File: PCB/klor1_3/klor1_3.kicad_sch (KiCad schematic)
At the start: 85 parts, among them J1 MJ-4PP-9, J2 Haptic Buzz, SW1 SW_PUSH-MX_W_LED, SW10 SW_PUSH-MX_W_LED, SW11 SW_PUSH-MX_W_LED, SW12 SW_PUSH-MX_W_LED, SW13 SW_PUSH-MX_W_LED, SW14 SW_PUSH-MX_W_LED, SW15 SW_PUSH-MX_W_LED, SW16 SW_PUSH-MX_W_LED, SW17 SW_PUSH-MX_W_LED, SW18 RotaryEncoder_Switch, SW19 SW_PUSH-MX_W_LED, SW2 SW_PUSH-MX_W_LED, SW20 SW_PUSH-MX_W_LED, SW21 SW_PUSH-MX_W_LED, SW23 5Way-Tactile_K1-1506DN-01, SW3 SW_PUSH-MX_W_LED, SW4 SW_PUSH-MX_W_LED, SW5 SW_PUSH-MX_W_LED, SW6 SW_PUSH-MX_W_LED, SW7 SW_PUSH-MX_W_LED, SW8 SW_PUSH-MX_W_LED, SW9 SW_PUSH-MX_W_LED, U1 ProMicro

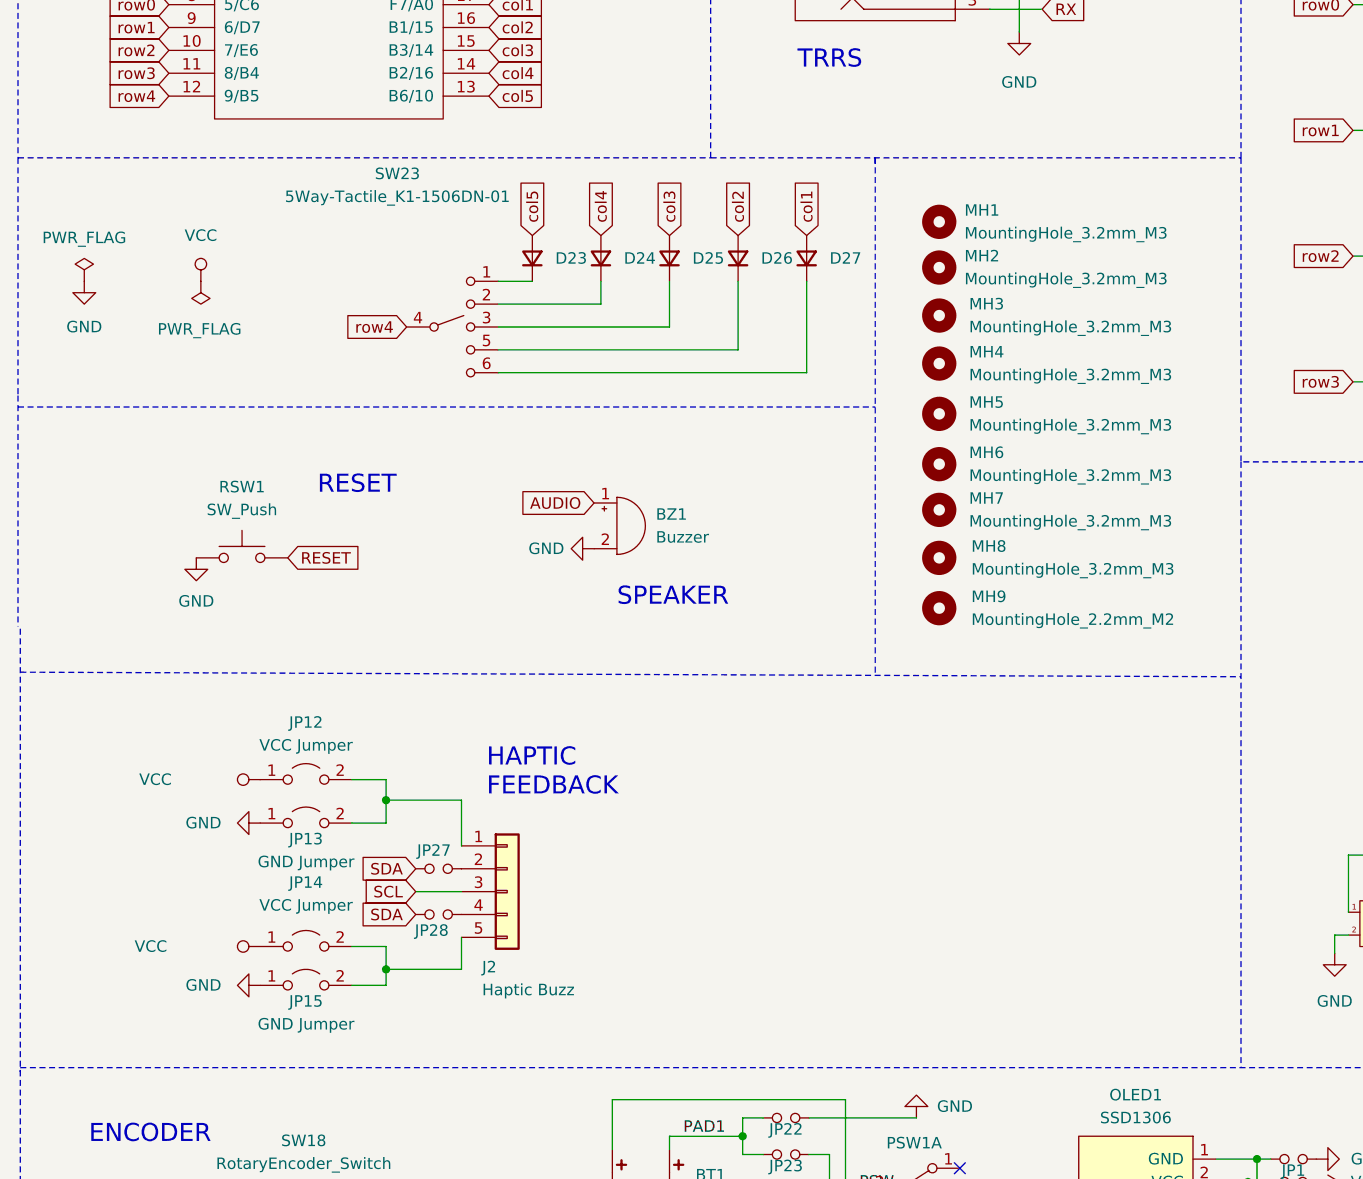
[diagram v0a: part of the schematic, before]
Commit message: move and add label for 5way switch in schematic
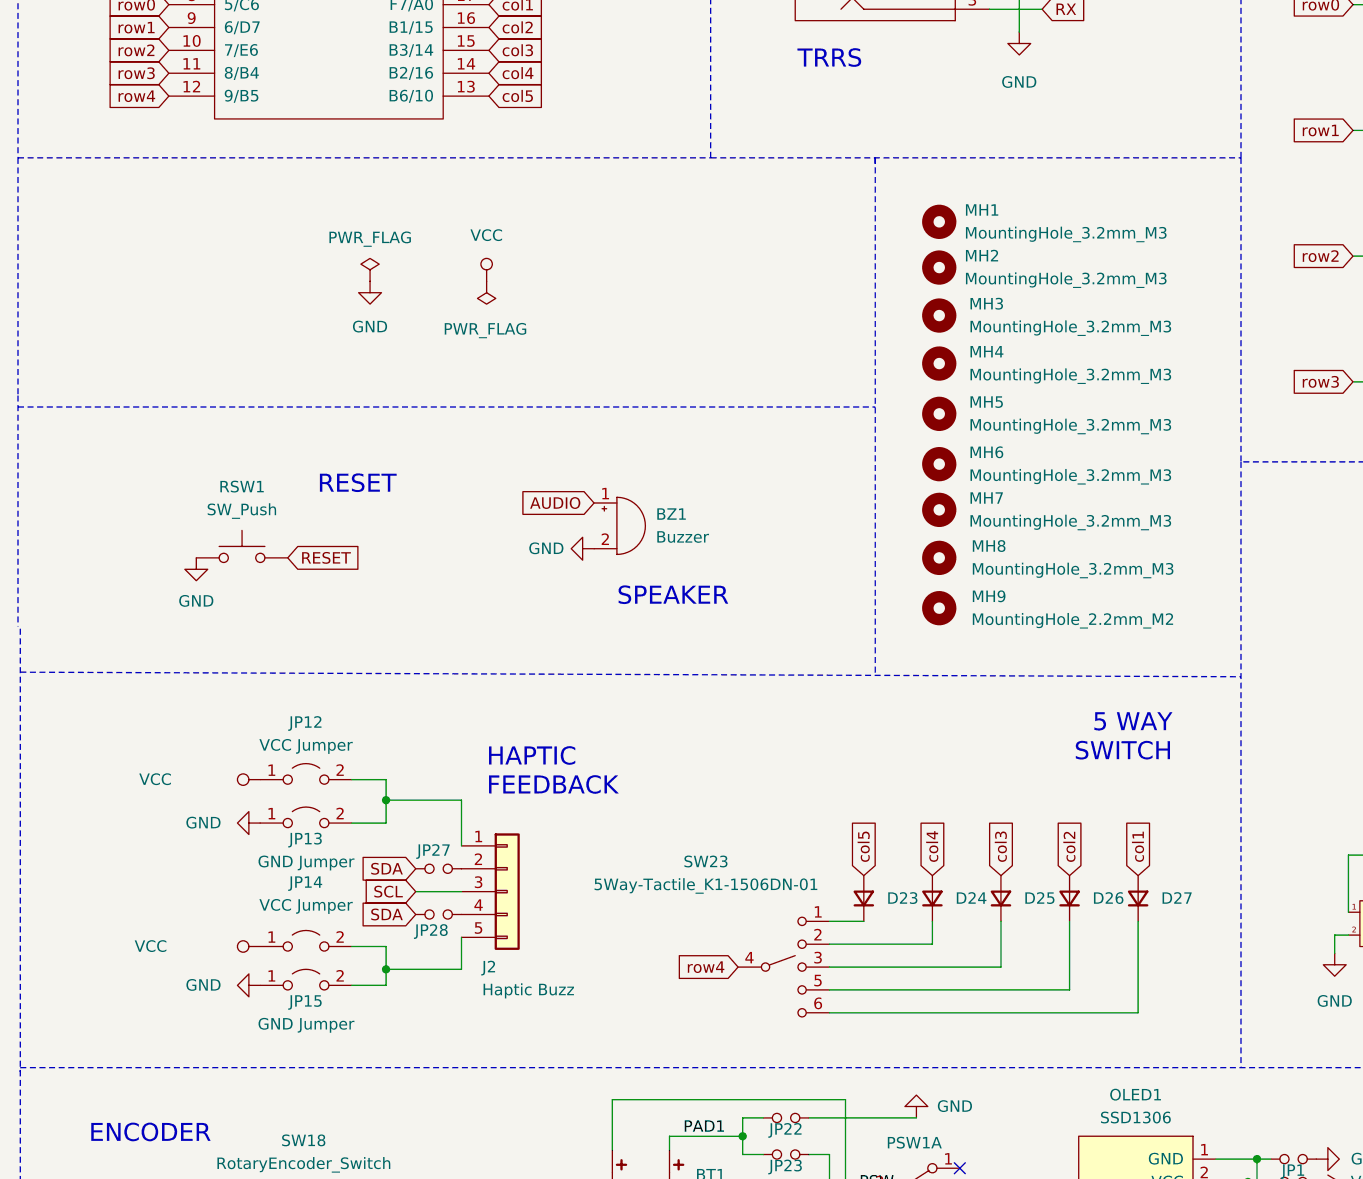
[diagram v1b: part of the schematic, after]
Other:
- note added: "5 WAY SWITCH"
- moved on the sheet: D23, D24, D25, D26, D27, SW23
